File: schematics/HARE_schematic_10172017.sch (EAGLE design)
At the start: 14 parts, among them IC1 NE5532N, IC2 NE5532N, IC3 FT232RL, J2 STEREOSWL, J3 STEREOSWL, SW1 3PDTBLUE, U1 ATMEGA328P-PU, X2 USB-B-H

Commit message: Updated schematic and board layout
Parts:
- added C1, C10, C13, C14, C15, C16, C17, C18, C2, C8, C9: 1uF, resistor:C-EUC0805K
- added C11, C12: 0.22uF, resistor:C-EUC0805K
- added C3: 10uF, resistor:C-EUC0805K
- added C4, C5, C6, C7: 0.01uF, resistor:C-EUC0805K
- added D1, D3, D4, D5: LED5MM, gm-diodes:LED5MM
- added D2: 1N4148-3, gm-diodes:1N4148-3
- added IC4: NE5532N, gm-ics:NE5532N
- added LDR1, LDR2, LDR3: (no value), gm-resistors:LDR5MM
- added R1: 470, rcl:R-US_M0805
- added R10, R11, R16, R18, R19, R2, R20, R21, R22, R23, R3, R4, R7, R8: 1k, resistor:R-US_R0805
- added R12, R9: 2.2k, resistor:R-US_R0805
- added R13: 47k, resistor:R-US_R0805
- added R14: 100k, resistor:R-US_R0805
- added R15, R17: 10k, resistor:R-US_R0805
- added R24, R25: 10k, resistor:R-TRIMM3314G
- added R5, R6: 10k, rcl:R-US_M0805
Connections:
- new net 5V: LDR1.2
- new net ADC_IN: R21.2
- new net BYPASS: SW1A.3, SW1C.3
- new net DAC_OUT: C8.2
- new net DRY: R22.2
- new net GND: APOT2.1, C3.1, C4.1, C7.1, D2.C, IC1P.V-, IC2P.V-, IC4P.V-, J1.3, J2.R, J2.RN, J2.S, J2.SN, J3.R, J3.RN, J3.S, J3.SN, LDR3.1, R17.1, R6.2, SW1B.2
- new net INPUT: J2.T, SW1A.2, SW1B.3
- new net N$10: C1.2, R2.2
- new net N$11: IC4A.-IN, R2.1, R3.2
- new net N$12: C4.2, R7.2, R8.1, R9.1
- new net N$13: C5.2, IC1A.-IN, R8.2
- new net N$14: C5.1, IC1A.OUT, R10.1, R9.2
- new net N$15: C8.1, R7.1
- new net N$16: C7.2, R10.2, R11.1, R12.1
- new net N$17: C6.2, IC1B.-IN, R11.2
- new net N$18: C6.1, C9.2, IC1B.OUT, R12.2
- new net N$19: J3.T, SW1C.1
- new net N$21: C10.1, R13.1
- new net N$22: C11.2, IC2A.-IN, R13.2, R14.1
- new net N$23: C13.2, IC2A.OUT, LDR2.2, R14.2, R15.2
- new net N$24: IC2A.+IN
- new net N$25: C12.1, LDR2.1, R15.1
- new net N$26: C10.2
- new net N$27: C11.1, C12.2, D2.A, R16.2
- new net N$28: IC2B.+IN
- new net N$29: LDR1.1, R16.1, R17.2
- new net N$30: C14.1, R18.1
- new net N$31: C15.2, LDR3.2, R18.2
- new net N$32: C15.1, R19.1
- new net N$33: IC2B.-IN, R19.2, R20.1
- new net N$34: C16.2, IC2B.OUT, R20.2
- new net N$35: C14.2
- new net N$36: C2.2, R21.1, R22.1
- new net N$37: C2.1, IC4A.OUT, R25.E
- new net N$38: IC4A.+IN
- new net N$39: C17.2
- new net N$40: C17.1, R4.1
- new net N$41: IC4B.-IN, R23.1, R4.2
- new net N$42: R23.2, R24.A, R24.S
- new net N$43: C18.2, IC4B.OUT, R24.E
- new net N$44: IC4B.+IN
- new net N$45: APOT2.3, C18.1
- new net N$46: APOT1.3, APOT2.2
- new net N$47: APOT1.2, SW1C.2
- new net N$48: APOT1.1
- new net N$49: R25.A, R25.S, R3.1
- new net N$7: D1.A, R1.2
- new net N$8: D1.C, SW1B.1
- new net N$9: C1.1, SW1A.1
- new net VCA_IN: C13.1
- new net VCA_OUT: C16.1
- new net VCC: IC1P.V+, IC2P.V+, IC4P.V+, J1.1, J1.2, R1.1, R5.1
- new net VCF_IN: C9.1
- new net V_BIAS: C3.2, IC1A.+IN, IC1B.+IN, R5.2, R6.1
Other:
- note added: "Analog Input Circuitry"
- note added: "Digital Processing Unit"
- note added: "PWMDAC Filter"
- note removed: "Analog Input"
- note removed: "Microcontroller"
- moved on the sheet: APOT1, APOT2, DPOT1, DPOT2, DPOT3, IC1A, IC1B, IC2A, IC2B, IC3, J1, J2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

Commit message: Updating first schematic build
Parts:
- added C19, C25: 10uF, resistor:C-EUC0805K
- added C20, C21: 22pF, resistor:C-EUC0805K
- added C22, C23, C24: 0.1uF, resistor:C-EUC0805K
- added IC5: 7805DT, gm-regulators:7805DT
- added Q1: 16 MHz, special:XTAL/S
- added R26, R27, R28: 1k, resistor:R-US_R0805
- added R29: 10k, resistor:R-US_R0805
- J2, J3: value STEREOSWL -> STEREOSW; device gm-jacks:STEREOSWL -> gm-jacks:STEREOSW
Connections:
- new net ADC1: DPOT1.2, U1.PC1
- new net ADC2: DPOT2.2, U1.PC2
- new net ADC3: DPOT3.2, U1.PC3
- new net N$50: IC3.TXD
- new net N$51: C21.2, Q1.1, U1.PB7
- new net N$52: IC3.USBDP, X2.D+
- new net N$53: IC3.USBDM, X2.D-
- new net N$54: C24.2, IC3.3V3OUT
- new net N$55: IC3.RXD
- new net N$56: R28.2, U1.PD6
- new net N$57: D5.A, R28.1
- new net N$58: R27.2, U1.PD5
- new net N$59: D4.A, R27.1
- new net N$60: R26.2, U1.PD3
- new net N$61: D3.A, R26.1
- new net N$62: IC3.!RESET, R29.2
- new net OSC: C20.2, Q1.2, U1.PB6
- new net RXD: U1.PD0
- new net TXD: U1.PD1
- net 5V: now also C19.2, C22.2, C23.2, DPOT1.3, DPOT2.3, DPOT3.3, IC3.VCC, IC5.VO, R29.1, U1.AVCC, U1.VCC, X2.VBUS
- net ADC_IN: now also U1.PC0
- net GND: now also C19.1, C20.1, C21.1, C22.1, C23.1, C24.1, C25.1, D3.C, D4.C, D5.C, DPOT1.1, DPOT2.1, DPOT3.1, IC3.GND, IC3.GND@1, IC3.GND@2, IC3.GND@A, IC3.TEST, IC5.GND, U1.GND_2, X2.GND
- net INPUT: now also J2.TN
- net N$19: now also J3.TN
- net VCC: now also C25.2, IC5.VI
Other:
- moved on the sheet: C3, D1, D3, D4, D5, DPOT1, DPOT2, DPOT3, IC3, J1, J3, R1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

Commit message: Update Schematic
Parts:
- added C26: 100nF, resistor:C-EUC0805K
- added D6, D7: LED5MM, gm-diodes:LED5MM
- added R30, R31, R32: 1k, resistor:R-US_R0805
- added R33: 10k, resistor:R-US_R0805
- added SW2: Reset Button, adafruit:SWITCH_PUSHBUTTONSOFTTOUCHSMD_SJ
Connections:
- removed net N$50: IC3.TXD
- removed net N$55: IC3.RXD
- new net CBUS1: D6.C
- new net CBUS2: D7.C
- new net CTS#: IC3.!CTS, U1.PD2
- new net N$63: D6.A, R30.2
- new net N$64: D7.A, R31.2
- new net N$65: IC3.CBUS2
- new net N$66: IC3.CBUS1
- new net N$68: IC3.VCCIO
- new net RESET#: R32.1, R33.2, SW2.P$2, U1.PC6
- new net RTS#: IC3.!RTS, R32.2
- new net VCCIO: R30.1, R31.1
- net 5V: now also C26.2, R33.1
- net GND: now also C26.1, SW2.P$1
- net RXD: now also IC3.RXD
- net TXD: now also IC3.TXD
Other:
- moved on the sheet: R29

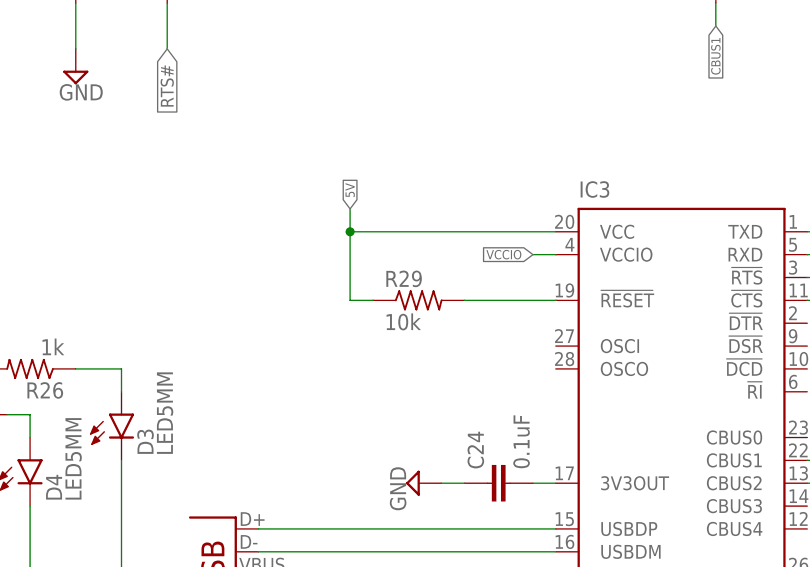
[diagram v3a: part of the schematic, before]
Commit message: Connected FT232 to reset switch.
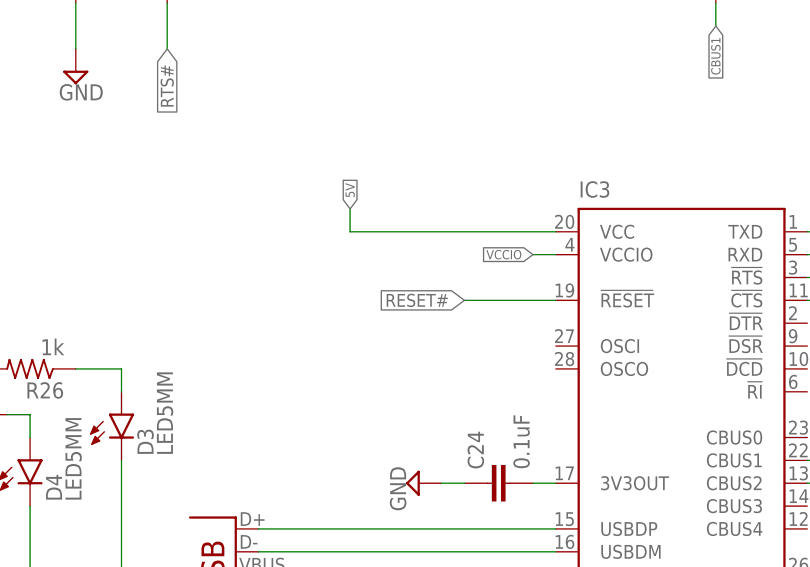
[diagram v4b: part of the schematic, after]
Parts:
- removed R29: 10k, resistor:R-US_R0805
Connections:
- net 5V: no longer R29.1
- net N$62: no longer R29.2
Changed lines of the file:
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@@
 <part name="SUPPLY30" library="supply2" deviceset="GND" device=""/>
 <part name="SUPPLY31" library="supply2" deviceset="GND" device=""/>
-<part name="R29" library="resistor" deviceset="R-US_" device="R0805" value="10k"/>
 <part name="D6" library="gm-diodes" deviceset="LED" device="5MM"/>
 <part name="D7" library="gm-diodes" deviceset="LED" device="5MM"/>
@@
 <instance part="SUPPLY30" gate="GND" x="142.24" y="180.34"/>
 <instance part="SUPPLY31" gate="GND" x="152.4" y="180.34"/>
-<instance part="R29" gate="G$1" x="185.42" y="213.36"/>
 <instance part="D6" gate="G$1" x="218.44" y="248.92" rot="R90"/>
 <instance part="D7" gate="G$1" x="231.14" y="248.92" rot="R90"/>
@@
 <wire x1="177.8" y1="220.98" x2="177.8" y2="223.52" width="0.1524" layer="91"/>
 <label x="177.8" y="223.52" size="1.016" layer="95" rot="R90" xref="yes"/>
-<pinref part="R29" gate="G$1" pin="1"/>
-<wire x1="180.34" y1="213.36" x2="177.8" y2="213.36" width="0.1524" layer="91"/>
-<wire x1="177.8" y1="213.36" x2="177.8" y2="220.98" width="0.1524" layer="91"/>
-<junction x="177.8" y="220.98"/>
 </segment>
 <segment>
@@
 <segment>
 <pinref part="IC3" gate="1" pin="!RESET"/>
-<pinref part="R29" gate="G$1" pin="2"/>
 <wire x1="200.66" y1="213.36" x2="190.5" y2="213.36" width="0.1524" layer="91"/>
 </segment>
@@
 <pinref part="SW2" gate="G$1" pin="P$2"/>
 <pinref part="R33" gate="G$1" pin="2"/>
-</segment>
-</net>
+<label x="190.5" y="213.36" size="1.4224" layer="95" rot="R180" xref="yes"/>
+</segment>
+</net>

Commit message: Added DAC_OUT node to schematic
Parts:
- added C27: 4.7nF, resistor:C-EUC0805K
- added R29: 1MEG, resistor:R-US_R0805
- added R34: 3.9k, resistor:R-US_R0805
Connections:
- removed net N$35: C14.2
- removed net N$39: C17.2
- new net N$50: R29.2, U1.PB2
- new net N$55: R34.2, U1.PB1
- net DAC_OUT: now also C27.2, R29.1, R34.1
- net GND: now also C27.1
- net VCA_IN: now also C14.2
- net VCA_OUT: now also C17.2
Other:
- moved on the sheet: APOT1, APOT2, C1, C10, C11, C12, C13, C14, C15, C16, C17, C18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

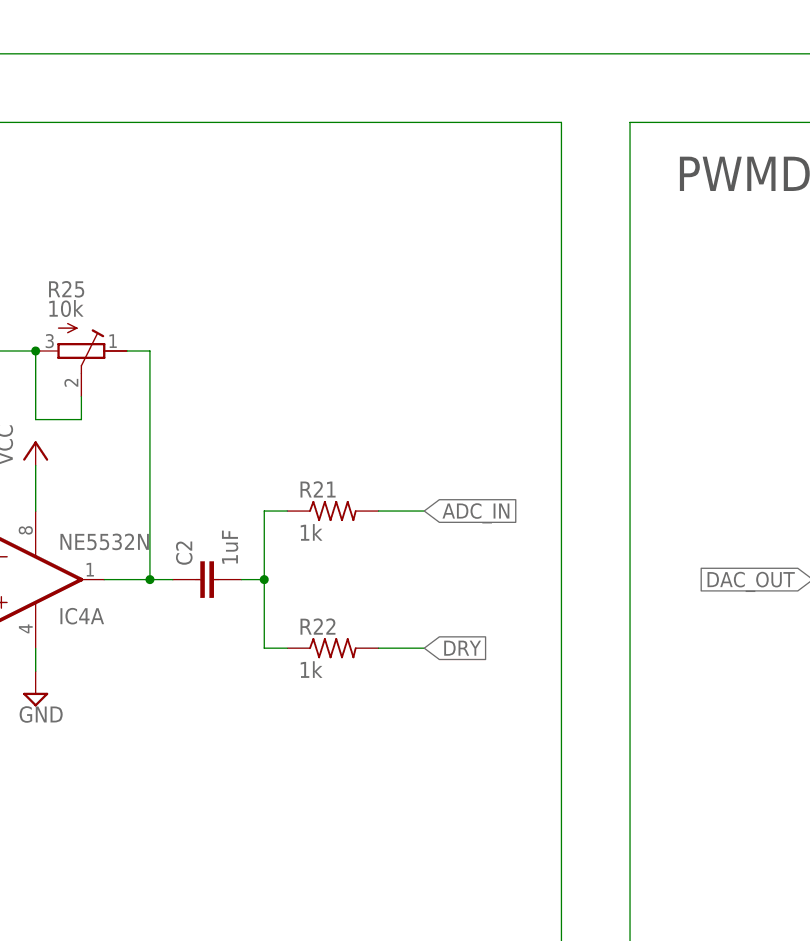
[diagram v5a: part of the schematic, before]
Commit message: Fixed ERC errors
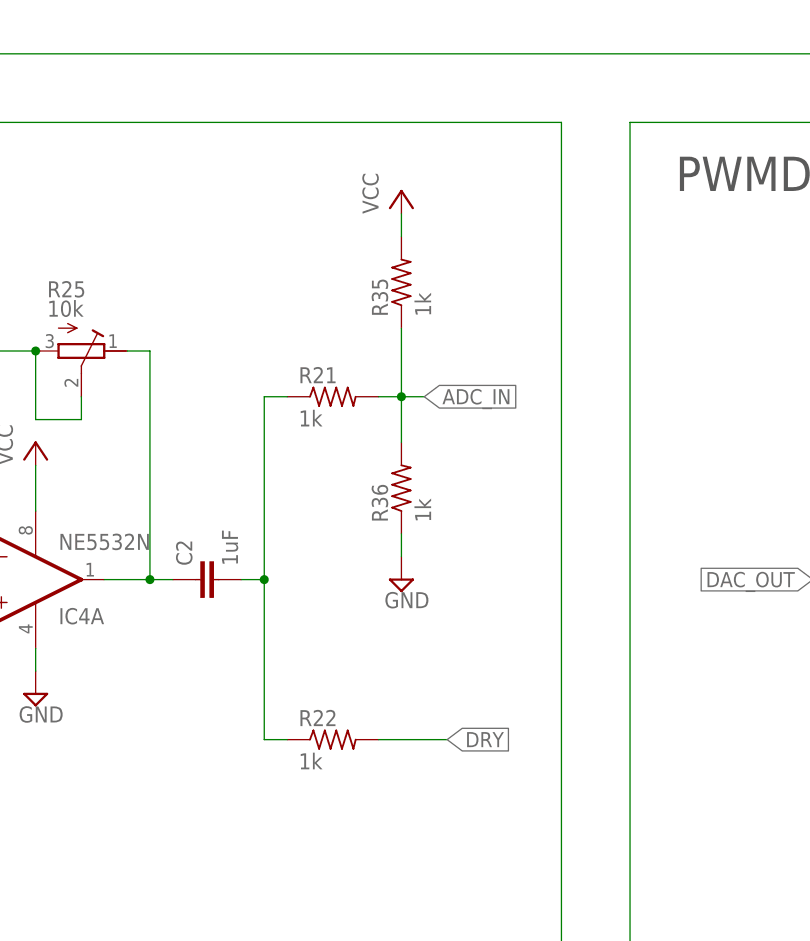
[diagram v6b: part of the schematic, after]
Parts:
- added R35, R36: 1k, resistor:R-US_R0805
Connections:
- removed net N$24: IC2A.+IN
- removed net N$28: IC2B.+IN
- removed net N$38: IC4A.+IN
- removed net N$44: IC4B.+IN
- removed net N$62: IC3.!RESET
- net ADC_IN: now also R35.1, R36.2
- net GND: now also R36.1
- net RESET#: now also IC3.!RESET
- net VCC: now also R35.2
- net V_BIAS: now also IC2A.+IN, IC2B.+IN, IC4A.+IN, IC4B.+IN
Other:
- moved on the sheet: R21, R22
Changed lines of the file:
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@@
 <part name="C27" library="resistor" deviceset="C-EU" device="C0805K" value="4.7nF"/>
 <part name="SUPPLY34" library="supply2" deviceset="GND" device=""/>
+<part name="R35" library="resistor" deviceset="R-US_" device="R0805" value="1k"/>
+<part name="R36" library="resistor" deviceset="R-US_" device="R0805" value="1k"/>
+<part name="SUPPLY35" library="supply2" deviceset="GND" device=""/>
+<part name="P+8" library="supply1" deviceset="VCC" device=""/>
 </parts>
 <sheets>
@@
 <instance part="C16" gate="G$1" x="678.18" y="73.66" rot="R270"/>
 <instance part="SUPPLY15" gate="GND" x="614.68" y="50.8"/>
-<instance part="R21" gate="G$1" x="149.86" y="83.82"/>
-<instance part="R22" gate="G$1" x="149.86" y="68.58"/>
+<instance part="R21" gate="G$1" x="149.86" y="96.52"/>
+<instance part="R22" gate="G$1" x="149.86" y="58.42"/>
 <instance part="IC4" gate="A" x="116.84" y="76.2" rot="MR180"/>
 <instance part="IC4" gate="P" x="116.84" y="76.2"/>
@@
 <instance part="C27" gate="G$1" x="63.5" y="187.96" rot="R180"/>
 <instance part="SUPPLY34" gate="GND" x="63.5" y="182.88"/>
+<instance part="R35" gate="G$1" x="157.48" y="109.22" rot="R90"/>
+<instance part="R36" gate="G$1" x="157.48" y="86.36" rot="R90"/>
+<instance part="SUPPLY35" gate="GND" x="157.48" y="76.2"/>
+<instance part="P+8" gate="VCC" x="157.48" y="119.38"/>
 </instances>
 <busses>
@@
 <pinref part="IC5" gate="A1" pin="VI"/>
 <wire x1="292.1" y1="182.88" x2="297.18" y2="182.88" width="0.1524" layer="91"/>
+</segment>
+<segment>
+<pinref part="R35" gate="G$1" pin="2"/>
+<pinref part="P+8" gate="VCC" pin="VCC"/>
+<wire x1="157.48" y1="114.3" x2="157.48" y2="116.84" width="0.1524" layer="91"/>
 </segment>
 </net>
@@
 <pinref part="SUPPLY34" gate="GND" pin="GND"/>
 </segment>
+<segment>
+<pinref part="SUPPLY35" gate="GND" pin="GND"/>
+<pinref part="R36" gate="G$1" pin="1"/>
+<wire x1="157.48" y1="78.74" x2="157.48" y2="81.28" width="0.1524" layer="91"/>
+</segment>
 </net>
 <net name="INPUT" class="0">
@@
 <label x="640.08" y="63.5" size="1.778" layer="95" rot="R270" xref="yes"/>
 <label x="762" y="60.96" size="1.778" layer="95" rot="R270" xref="yes"/>
+</segment>
+<segment>
+<wire x1="480.06" y1="43.18" x2="480.06" y2="50.8" width="0.1524" layer="91"/>
+<pinref part="IC2" gate="A" pin="+IN"/>
+<wire x1="480.06" y1="50.8" x2="490.22" y2="50.8" width="0.1524" layer="91"/>
+</segment>
+<segment>
+<pinref part="IC2" gate="B" pin="+IN"/>
+<wire x1="647.7" y1="71.12" x2="640.08" y2="71.12" width="0.1524" layer="91"/>
+<wire x1="640.08" y1="71.12" x2="640.08" y2="63.5" width="0.1524" layer="91"/>
+</segment>
+<segment>
+<wire x1="762" y1="60.96" x2="762" y2="66.04" width="0.1524" layer="91"/>
+<pinref part="IC4" gate="B" pin="+IN"/>
+<wire x1="762" y1="66.04" x2="767.08" y2="66.04" width="0.1524" layer="91"/>
+</segment>
+<segment>
+<wire x1="104.14" y1="66.04" x2="104.14" y2="73.66" width="0.1524" layer="91"/>
+<pinref part="IC4" gate="A" pin="+IN"/>
+<wire x1="104.14" y1="73.66" x2="109.22" y2="73.66" width="0.1524" layer="91"/>
 </segment>
 </net>
@@
 </segment>
 </net>
-<net name="N$24" class="0">
-<segment>
-<wire x1="480.06" y1="43.18" x2="480.06" y2="50.8" width="0.1524" layer="91"/>
-<pinref part="IC2" gate="A" pin="+IN"/>
-<wire x1="480.06" y1="50.8" x2="490.22" y2="50.8" width="0.1524" layer="91"/>
-</segment>
-</net>
 <net name="N$26" class="0">
 <segment>
@@
 </segment>
 </net>
-<net name="N$28" class="0">
-<segment>
-<pinref part="IC2" gate="B" pin="+IN"/>
-<wire x1="647.7" y1="71.12" x2="640.08" y2="71.12" width="0.1524" layer="91"/>
-<wire x1="640.08" y1="71.12" x2="640.08" y2="63.5" width="0.1524" layer="91"/>
-</segment>
-</net>
 <net name="N$30" class="0">
 <segment>
@@
 <segment>
 <pinref part="R21" gate="G$1" pin="2"/>
-<wire x1="154.94" y1="83.82" x2="160.02" y2="83.82" width="0.1524" layer="91"/>
-<label x="160.02" y="83.82" size="1.6764" layer="95" xref="yes"/>
+<wire x1="154.94" y1="96.52" x2="157.48" y2="96.52" width="0.1524" layer="91"/>
+<label x="160.02" y="96.52" size="1.6764" layer="95" xref="yes"/>
+<pinref part="R36" gate="G$1" pin="2"/>
+<wire x1="157.48" y1="96.52" x2="160.02" y2="96.52" width="0.1524" layer="91"/>
+<wire x1="157.48" y1="91.44" x2="157.48" y2="96.52" width="0.1524" layer="91"/>
+<junction x="157.48" y="96.52"/>
+<pinref part="R35" gate="G$1" pin="1"/>
+<wire x1="157.48" y1="96.52" x2="157.48" y2="104.14" width="0.1524" layer="91"/>
 </segment>
 <segment>
@@
 <segment>
 <pinref part="R22" gate="G$1" pin="2"/>
-<wire x1="154.94" y1="68.58" x2="160.02" y2="68.58" width="0.1524" layer="91"/>
-<label x="160.02" y="68.58" size="1.6764" layer="95" xref="yes"/>
+<wire x1="154.94" y1="58.42" x2="162.56" y2="58.42" width="0.1524" layer="91"/>
+<label x="162.56" y="58.42" size="1.6764" layer="95" xref="yes"/>
 <label x="830.58" y="88.9" size="1.6764" layer="95" xref="yes"/>
 </segment>
@@
 <pinref part="R22" gate="G$1" pin="1"/>
 <pinref part="R21" gate="G$1" pin="1"/>
-<wire x1="142.24" y1="83.82" x2="144.78" y2="83.82" width="0.1524" layer="91"/>
-<wire x1="142.24" y1="83.82" x2="142.24" y2="76.2" width="0.1524" layer="91"/>
-<wire x1="142.24" y1="76.2" x2="142.24" y2="68.58" width="0.1524" layer="91"/>
-<wire x1="142.24" y1="68.58" x2="144.78" y2="68.58" width="0.1524" layer="91"/>
+<wire x1="142.24" y1="96.52" x2="144.78" y2="96.52" width="0.1524" layer="91"/>
+<wire x1="142.24" y1="96.52" x2="142.24" y2="76.2" width="0.1524" layer="91"/>
+<wire x1="142.24" y1="76.2" x2="142.24" y2="58.42" width="0.1524" layer="91"/>
+<wire x1="142.24" y1="58.42" x2="144.78" y2="58.42" width="0.1524" layer="91"/>
 <pinref part="C2" gate="G$1" pin="2"/>
 <wire x1="139.7" y1="76.2" x2="142.24" y2="76.2" width="0.1524" layer="91"/>
@@
 </segment>
 </net>
-<net name="N$38" class="0">
-<segment>
-<wire x1="104.14" y1="66.04" x2="104.14" y2="73.66" width="0.1524" layer="91"/>
-<pinref part="IC4" gate="A" pin="+IN"/>
-<wire x1="104.14" y1="73.66" x2="109.22" y2="73.66" width="0.1524" layer="91"/>
-</segment>
-</net>
 <net name="N$40" class="0">
 <segment>
@@
 <wire x1="789.94" y1="68.58" x2="795.02" y2="68.58" width="0.1524" layer="91"/>
 <junction x="789.94" y="68.58"/>
-</segment>
-</net>
-<net name="N$44" class="0">
-<segment>
-<wire x1="762" y1="60.96" x2="762" y2="66.04" width="0.1524" layer="91"/>
-<pinref part="IC4" gate="B" pin="+IN"/>
-<wire x1="762" y1="66.04" x2="767.08" y2="66.04" width="0.1524" layer="91"/>
 </segment>
 </net>
@@
 </segment>
 </net>
-<net name="N$62" class="0">
-<segment>
-<pinref part="IC3" gate="1" pin="!RESET"/>
-<wire x1="200.66" y1="208.28" x2="190.5" y2="208.28" width="0.1524" layer="91"/>
-</segment>
-</net>
 <net name="N$63" class="0">
 <segment>
@@
 <label x="190.5" y="208.28" size="1.4224" layer="95" rot="R180" xref="yes"/>
 </segment>
-</net>
+<segment>
+<pinref part="IC3" gate="1" pin="!RESET"/>
+<wire x1="200.66" y1="208.28" x2="190.5" y2="208.28" width="0.1524" layer="91"/>
+</segment>
+</net>

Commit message: Resolved errors and most warnings in ERC
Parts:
- added R37, R38: 1k, resistor:R-US_R0805
- APOT1, DPOT1, DPOT2, DPOT3, LDR1, LDR2, LDR3: value (none) -> 100k
- APOT2: value (none) -> 250k
- J1: value (none) -> 9V
- R35, R36: value 1k -> 10k
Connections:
- removed net N$26: C10.2
- removed net N$48: APOT1.1
- removed net N$65: IC3.CBUS2
- removed net N$66: IC3.CBUS1
- removed net N$68: IC3.VCCIO
- new net N$24: IC3.!DCD, IC3.!DSR, IC3.!DTR, IC3.!RI, R37.2
- new net N$28: IC3.OSCI, R38.2
- net 5V: now also U1.AREF
- net CBUS1: now also IC3.CBUS1
- net CBUS2: now also IC3.CBUS2
- net DRY: now also APOT1.1
- net GND: now also R37.1, R38.1
- net VCCIO: now also IC3.VCCIO
- net VCF_IN: now also C10.2
